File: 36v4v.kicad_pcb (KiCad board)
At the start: 2 copper layers, 85.1 x 48 mm, 45 parts, among them J1 Conn_01x03, J2 Conn_01x02, J3 Conn_01x02, J4 Conn_01x02, J5 Conn_01x02, U1 InnoSwitch3-CE, INN3162C, inS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

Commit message: More changes as per AA
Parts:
- added J6: Conn_01x02, Connector_PinHeader_2.54mm:PinHeader_1x02_P2.54mm_Vertical, F.Cu at (185.8, 100.0)
- added J7: Conn_01x02, Connector_PinHeader_2.54mm:PinHeader_1x02_P2.54mm_Vertical, F.Cu at (185.8, 92.9)
- D7: footprint Diode_THT:D_DO-15_P10.16mm_Horizontal -> Diode_THT:D_DO-27_P5.08mm_Vertical_AnodeUp
- F1: footprint Fuse:Fuse_0805_2012Metric -> Fuse:Fuseholder_Cylinder-5x20mm_Schurter_0031_8201_Horizontal_Open
- moved F1 26.7 mm to (126.5, 78.0), turned to 270 degrees
- moved RV1 17.1 mm to (119.6, 84.0), turned to 180 degrees
- moved C2 7.09 mm to (134.7, 81.2)
- moved D7 6.39 mm to (177.6, 97.5)
- moved C1 5.66 mm to (134.8, 97.7)
- moved C4 4.96 mm to (136.2, 88.7), turned to 90 degrees
- moved R4 4.50 mm to (140.0, 88.5)
- moved R8 3.91 mm to (179.1, 104.6)
- moved R7 3.76 mm to (176.9, 101.7)
- moved C8 3.31 mm to (176.1, 106.4)
- moved R2 3.02 mm to (144.4, 75.5)
- moved D5 3.01 mm to (144.3, 85.9)
- moved C6 2.68 mm to (159.5, 87.5)
- moved C5 2.54 mm to (159.4, 90.5)
- moved C13 2.54 mm to (171.3, 75.5)
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- renumbered C9 to C10, C10 to C11, C11 to C12, C12 to C13, C5A1 to C6, C6 to C7, C7 to C8, C8 to C9, R11a1 to R11, R11b1 to R12
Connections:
- J4 pad 1: (no net) -> Net-(J4-Pad1)
- J4 pad 2: (no net) -> Net-(J4-Pad2)
- J5 pad 1: (no net) -> Net-(J5-Pad1)
- J5 pad 2: (no net) -> Net-(J5-Pad2)
- RV1 pad 1: Net-(F1-Pad2) -> Net-(F1-Pad1)
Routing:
- net Earth: track 91.7 -> 67.2 mm, vias 1 -> 2
- net GND: track 95.7 -> 73.7 mm, vias 4 -> 3
- net Net-(F1-Pad1): track 15.6 -> 32.0 mm
- net Net-(D3-Pad2): track 43.4 -> 56.0 mm, vias 1 -> 0
- net Net-(J4-Pad2): track 0.00 -> 11.3 mm
- net Net-(C1-Pad1): track 44.4 -> 54.9 mm, vias 0 -> 1
- net Net-(C2-Pad1): track 76.1 -> 66.5 mm, vias 0 -> 1
- net Net-(J4-Pad1): track 0.00 -> 9.45 mm
- net Net-(J5-Pad2): track 0.00 -> 7.92 mm
- net Net-(C1-Pad2): track 41.1 -> 48.6 mm, vias 1 -> 2
- net Net-(J5-Pad1): track 0.00 -> 6.51 mm
- net Net-(C4-Pad1): track 28.5 -> 34.4 mm
- net /GND1: track 35.2 -> 31.5 mm
- net /36V: track 25.1 -> 21.6 mm
- net /4V: track 55.8 -> 53.3 mm
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
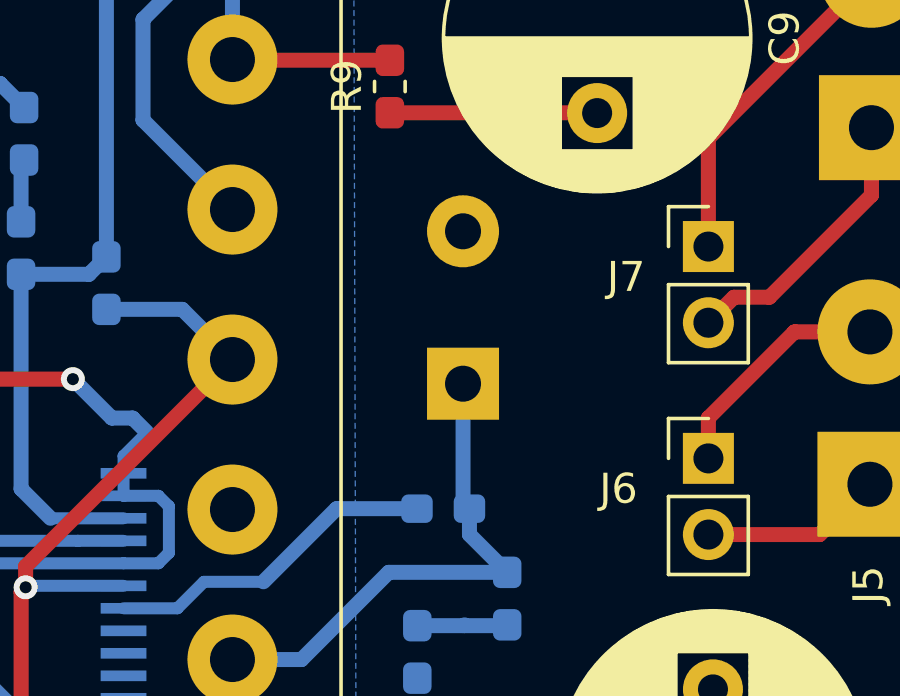
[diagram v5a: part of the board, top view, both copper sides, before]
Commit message: Diode footprint change
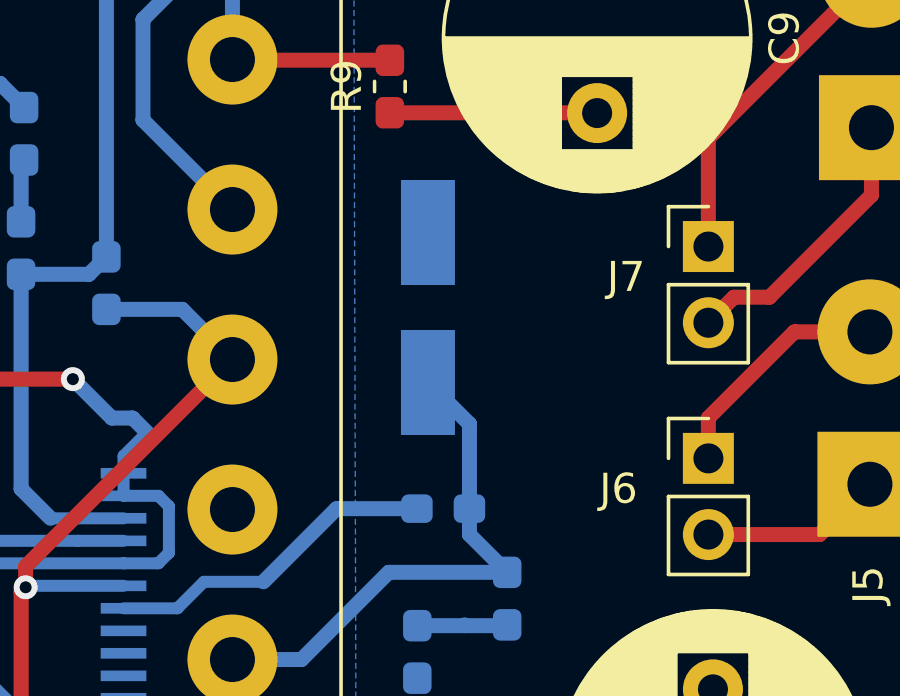
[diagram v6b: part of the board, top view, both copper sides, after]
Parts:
- D7: footprint Diode_THT:D_DO-27_P5.08mm_Vertical_AnodeUp -> Diode_SMD:D_SMA_Handsoldering
- moved D7 2.80 mm to (176.4, 94.9)
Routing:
- net Net-(D7-Pad1): track 17.3 -> 18.1 mm

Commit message: Rotated U1 in schematic to make primary/secondary clearer
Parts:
- turned C5 to 0 degrees
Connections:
- C5 pad 1: GND -> Net-(C5-Pad1)
- C5 pad 2: Net-(C5-Pad2) -> GND
- C6 pad 2: Net-(C5-Pad2) -> Net-(C5-Pad1)
- U1 pad 4: Net-(C5-Pad2) -> Net-(C5-Pad1)
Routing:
- net Net-(C5-Pad2): track 21.6 -> 0.00 mm
- net Net-(C5-Pad1): track 0.00 -> 21.6 mm

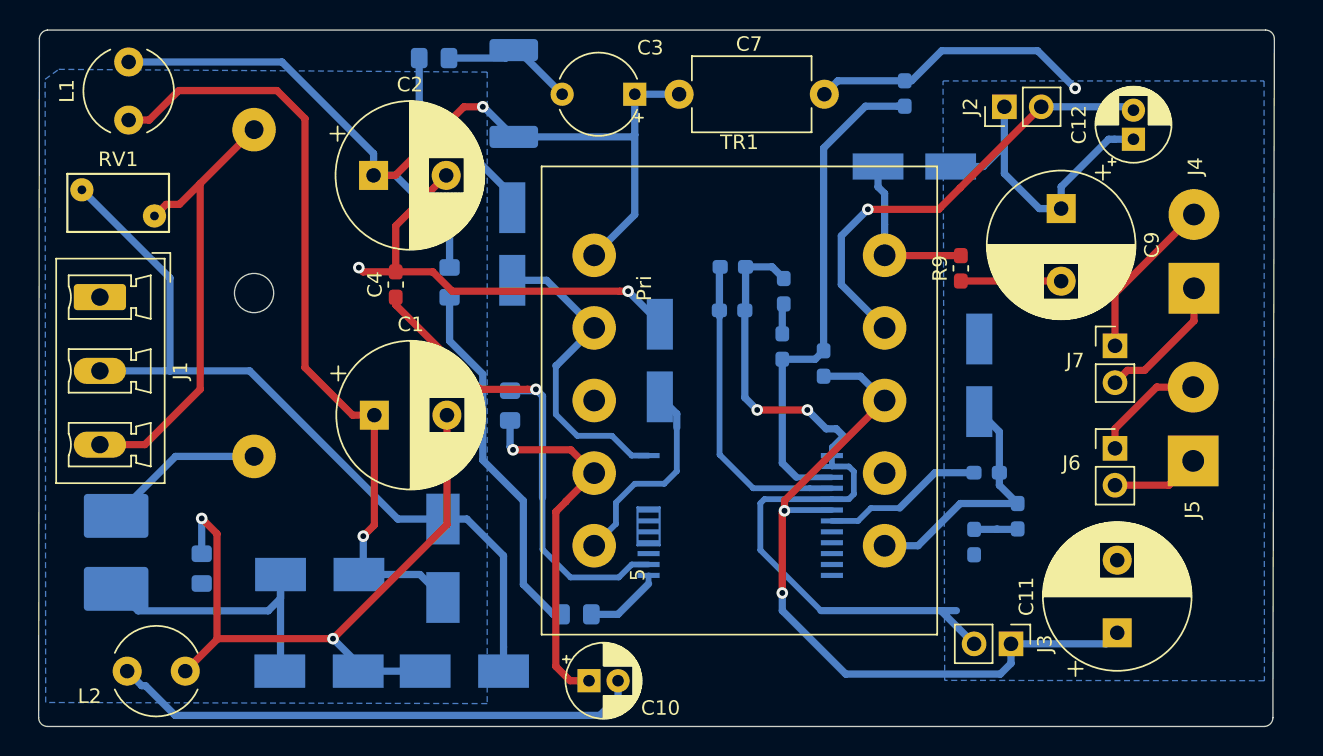
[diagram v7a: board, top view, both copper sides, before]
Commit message: Added 36V zone on back Cu to minimize loop area formed by secondary winding, output rectifier (D8) and output filter cap (C9)
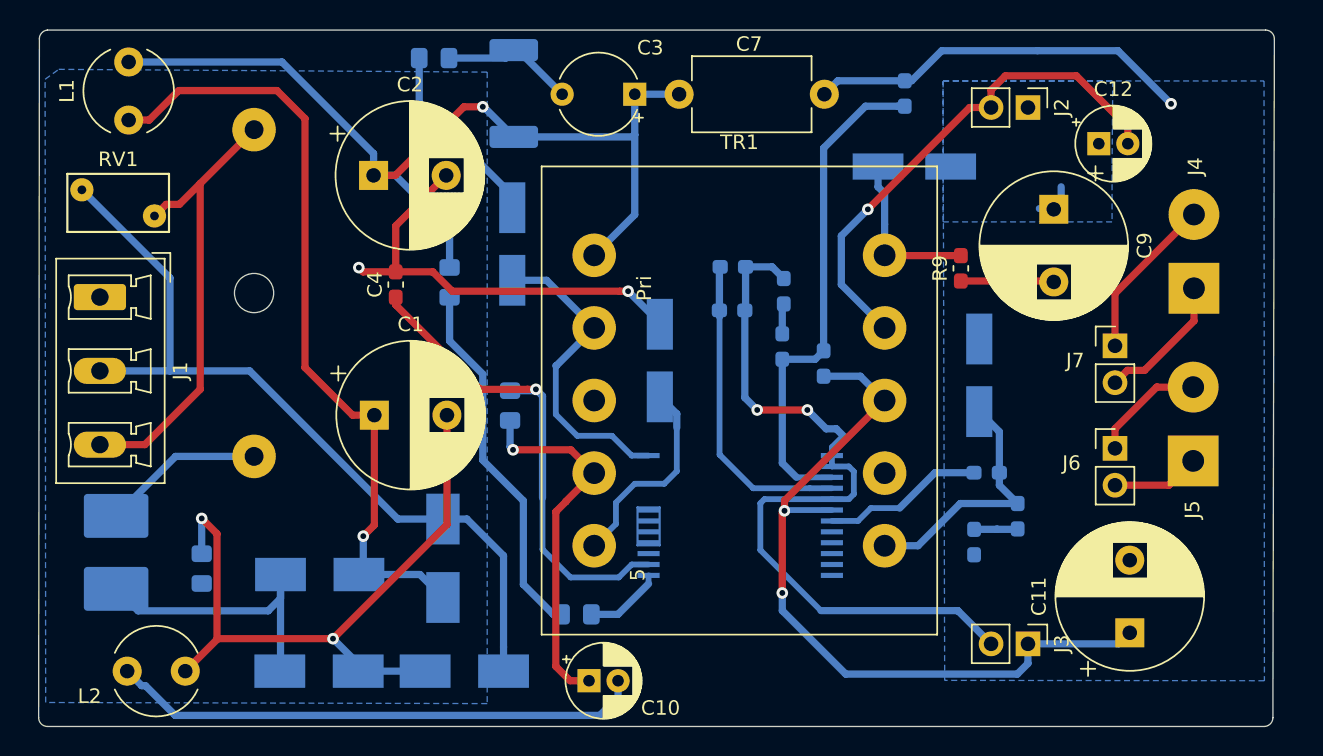
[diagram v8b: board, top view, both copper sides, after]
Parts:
- moved C12 2.41 mm to (184.7, 79.0), turned to 0 degrees
- moved J2 1.63 mm to (179.8, 76.5), turned to 270 degrees
- moved J3 1.17 mm to (179.8, 113.4)
- moved C11 0.86 mm to (186.8, 112.7)
- moved C9 0.51 mm to (181.6, 83.5)
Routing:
- net /36V: track 21.6 -> 3.00 mm
- net GND: track 73.7 -> 80.7 mm
- net /GND1: track 31.5 -> 35.2 mm
- net /4V: track 53.3 -> 54.1 mm
- added copper zone on B.Cu, net /36V
